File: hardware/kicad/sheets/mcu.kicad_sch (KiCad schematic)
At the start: 37 parts, among them J1 USB-C, J14 QWIIC, J5 DISPLAY, J6 NAV_SW, J7 AUX, SW1 RESET, SW2 BOOT, U1 ESP32-S3-WROOM-1U-N16R2, U4 SRV05-4

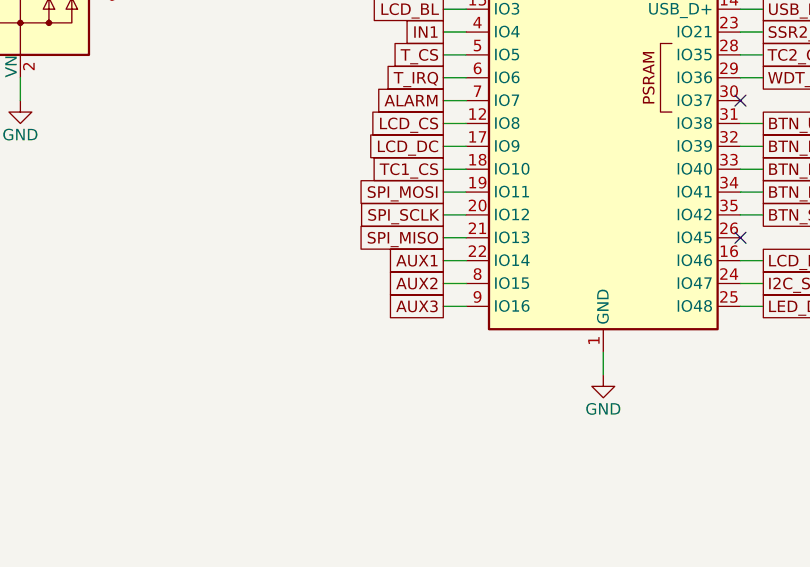
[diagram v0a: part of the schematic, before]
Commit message: hardware: uncross the AUX bank - vent on GPIO16, U6 channels reversed
U6's outputs sit level with their inputs, so channel 1 (pins 1/16, the
bottom of the SOIC) fed J10.2 at the top of the terminal and all three
output traces crossed, two of them through B.Cu. AUX1 now uses channel 3
and AUX3 channel 1, so O3/O2/O1 fan straight across to J10.2/3/4 on F.Cu
with no via (was 1/1/0 vias).

The input copper was already in the order the board's geography forces:
U6's top input escapes by the B.Cu lane north to U1 pin 9, the bottom
one by the route south of LCD_CS to U1 pin 22. Rather than re-route it,
the GPIOs follow it: vent (AUX1) moves GPIO14 -> GPIO16, AUX3 moves
GPIO16 -> GPIO14, AUX2 stays on GPIO15. The existing input tracks keep
their geometry under the swapped names, and R23/R25 trade places so each
pulldown stays on the input it terminates. U6->J10 is wired by label
pairs now, since the schematic can't draw the swap without a crossing.

Kconfig defaults, pin-assignments, the roadmap, the KiCad README and
DESIGN-NOTES follow. An existing local sdkconfig keeps the old values
until KILN_PIN_VENT / KILN_PIN_AUX3 are reset.

Co-Authored-By: Claude Opus 5.5 <noreply@anthropic.com>
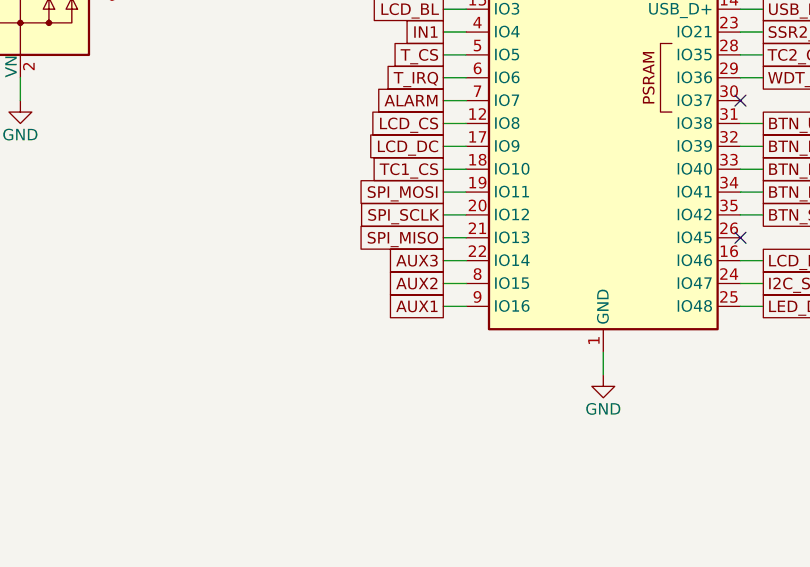
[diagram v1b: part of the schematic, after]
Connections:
- net AUX1: now also U1.9 (IO16); no longer U1.22 (IO14)
- net AUX3: now also U1.22 (IO14); no longer U1.9 (IO16)

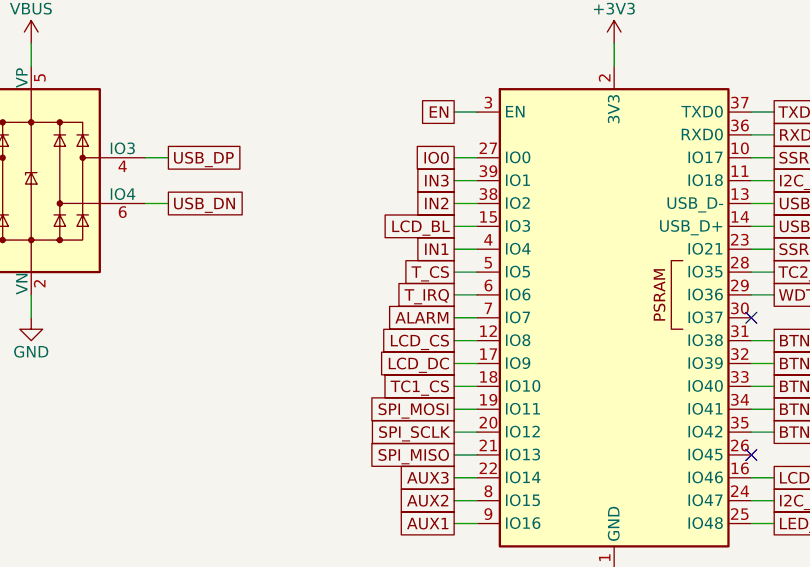
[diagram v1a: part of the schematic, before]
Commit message: hardware: TC1_CS and IN3 trade GPIOs, D5 channels follow the copper
TC1_CS kept rev A's TC_CS pad through the rename - U1 pin 18, on the
module's bottom edge - so it ran back up under U1 on B.Cu to reach U3 at
the top right, while IN3 left pin 39 at the top right and came all the
way down to its filter block at the bottom left. The two crossed and each
ran the long way round. They now trade pins: TC1_CS on pin 39 (GPIO1),
IN3 on pin 18 (GPIO10). IN3 stays on an ADC1-capable GPIO, so the
resistance-monitored interlock is still possible without a respin.
TC1_CS + IN3: 197 mm / 11 vias -> 167 mm / 5.

D5's four SRV05-4 channels are interchangeable, like U6's. IN3_RAW sat on
IO3 (pin 4), on the side facing J11, and crossed IN2_RAW through 3 vias
to reach R28 west of D5. IN2_RAW now uses the idle IO4 (pin 6), IN3_RAW
IO2 (pin 3), and IO3 is the idle one: IN3_RAW is 0 vias, all F.Cu.

Across the five nets (TC1_CS, IN3, IN1/2/3_RAW): 287 mm / 18 vias ->
260 mm / 7. Board copper changes only on those nets, five pads re-netted,
no part moved, silk unchanged.

Kconfig defaults (KILN_PIN_TC1_CS 10 -> 1, KILN_PIN_IN_SPARE 1 -> 10),
pin-assignments, DESIGN-NOTES and the firmware backlog follow; the
backlog's AUX row was also still on the pre-#368 numbers. An existing
local sdkconfig keeps the old values until those two are reset.

Co-Authored-By: Claude Opus 5.5 <noreply@anthropic.com>
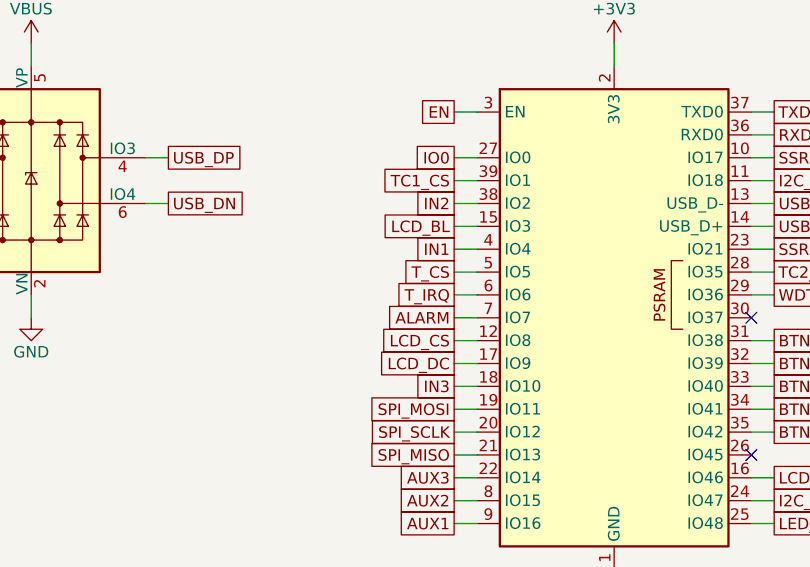
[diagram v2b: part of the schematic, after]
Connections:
- net IN3: now also U1.18 (IO10); no longer U1.39 (IO1)
- net TC1_CS: now also U1.39 (IO1); no longer U1.18 (IO10)

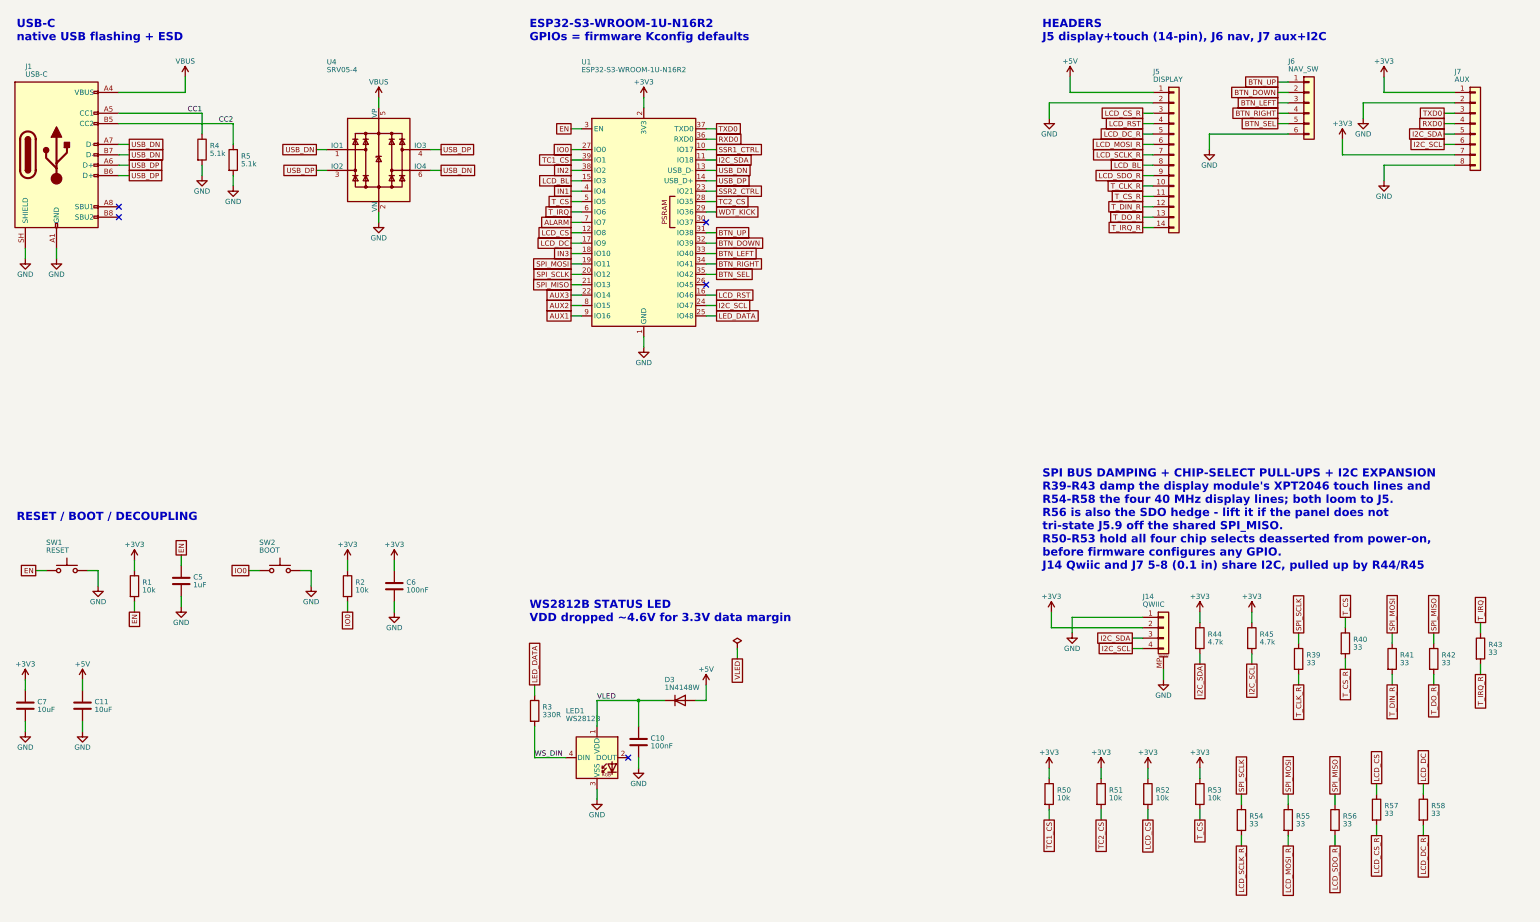
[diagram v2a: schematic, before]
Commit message: hardware: hierarchical schematic, ERC at 0/0, rev B.3
Applies items 1-3 of SCHEMATIC-REVIEW-2026-10-22.md.

ERC: the 173 lib_symbol_mismatch warnings were over-escaped quotes in the
embedded power symbols' Description strings; refreshed from the library.
The 18 off-grid power symbols are snapped and their stub wires redrawn.
The VIN and VLED global labels that existed only to carry a PWR_FLAG are
gone; the flags now sit on the nets they drive (J2.1, the VLED junction).
ERC reads 0 errors / 0 warnings with the documented SDO exclusion.

Hierarchy: no global labels remain. Each net that crosses sheets has one
hierarchical label per sheet, matching sheet pins on the root, and the
root wires those pins as a block diagram. Every other former global label
is a local label. The eight signal test points (TP4-TP11) move from the
test sheet to the mcu and ct sheets beside their nets, so the test block
needs no pins. KiCad names the nets /mcu/SPI_MISO etc.; netlist.py strips
the path, so the board's net names and the routing tables are unchanged
(182 components, 538 pads, 0 mismatches). single_global_label is now a
warning. check_sync_idempotent's collision fixture used the bare
"SPI_MISO" name and is updated, with a loud failure if its victims vanish.

Drawing: rev B.3 dated 2026-10-22 on every sheet, ct on A3 like the rest,
the three overflowing titles shortened, and the notes no longer refer to
design.py or to crystal load caps that no longer exist.

Co-Authored-By: Claude Fable 5.1 <noreply@anthropic.com>
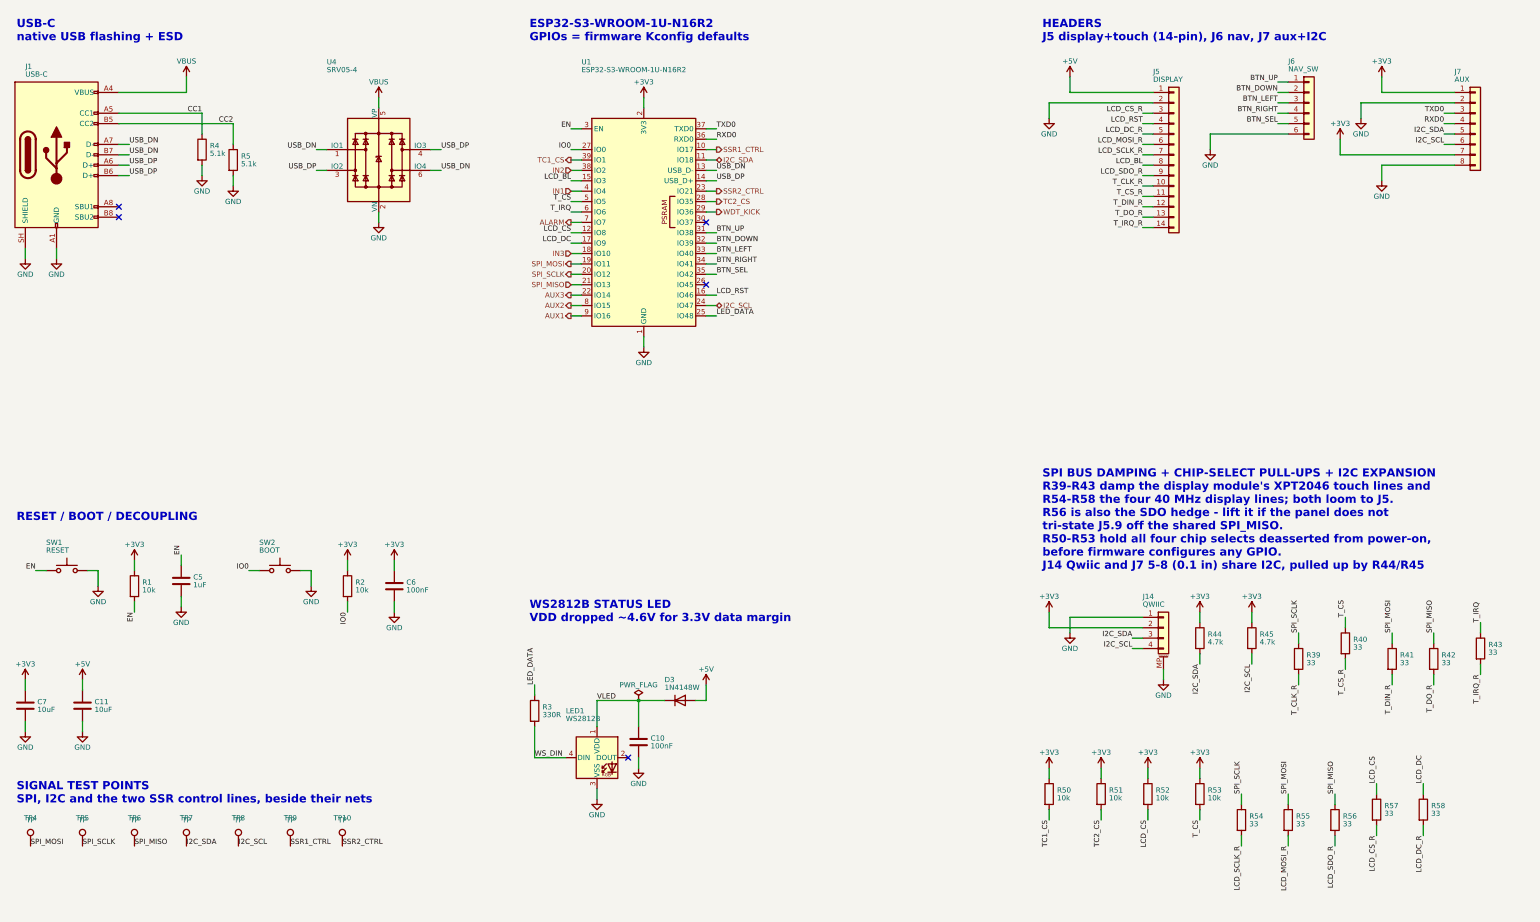
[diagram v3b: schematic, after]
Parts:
- added TP10, TP4, TP5, TP6, TP7, TP8, TP9: TP, TestPoint:TestPoint_Pad_D1.0mm, symbol Connector:TestPoint
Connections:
- net I2C_SCL: now also TP8.1
- net I2C_SDA: now also TP7.1
- net SPI_MISO: now also TP6.1
- net SPI_MOSI: now also TP4.1
- net SPI_SCLK: now also TP5.1
- net SSR1_CTRL: now also TP9.1
- net SSR2_CTRL: now also TP10.1
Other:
- note added: "SIGNAL TEST POINTS SPI, I2C and the two SSR control lines, beside their nets"
- title: Bisque Kiln Controller - ESP32-S3, USB, reset, status LED, headers, bus damping -> Bisque Kiln Controller - ESP32-S3, USB, headers, status LED
